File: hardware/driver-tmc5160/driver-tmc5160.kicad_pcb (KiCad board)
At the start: 2 copper layers, 30 x 27 mm, 54 parts, among them M1 Micro-Fit 3.0, T1 GND, T10 STEP, T11 GND, T12 DIR, T13 EN, T16 DIAG0, T17 DIAG1, T18 ENCA, T19 ENCB, T2 CLK, T20 ENCN, T3 12V, T4 SCK, T5 GND, T6 SDI, T7 SDO, T8 VCC, T9 CS0, U1 TMC5160A-TA

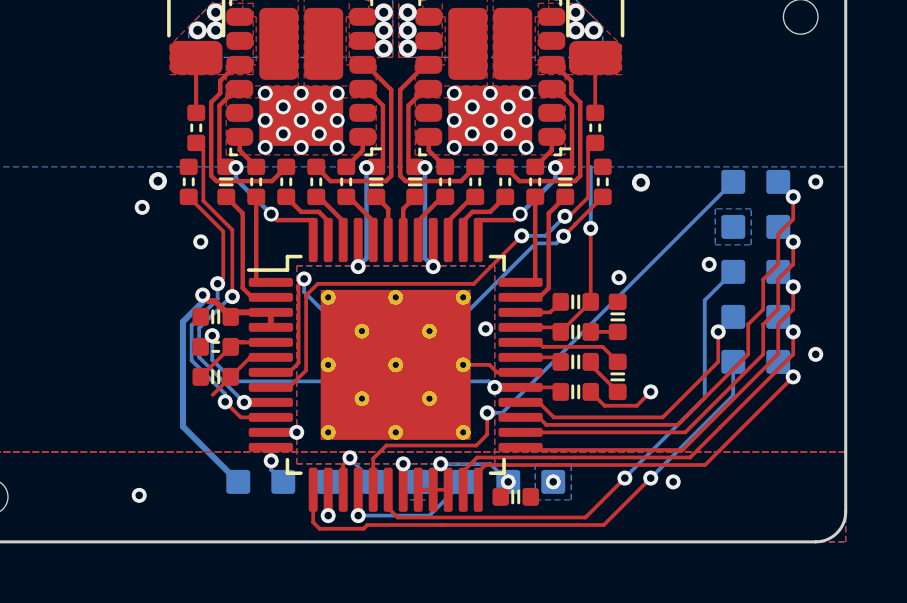
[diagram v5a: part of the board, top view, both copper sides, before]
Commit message: added components and further work on PCB layout design
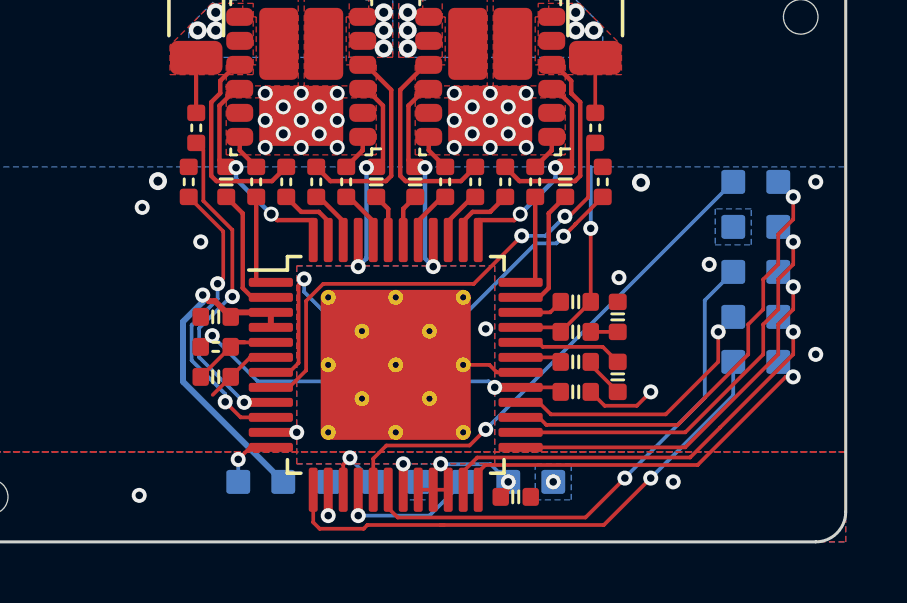
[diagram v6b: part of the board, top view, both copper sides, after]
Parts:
- moved T2 1.50 mm to (129.8, 84.5), turned to 0 degrees
- moved T3 1.50 mm to (131.2, 84.5), turned to 0 degrees
- turned T4 to 0 degrees
- turned T5 to 0 degrees
- turned T6 to 0 degrees
- turned T7 to 0 degrees
- turned T8 to 0 degrees
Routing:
- net +12V: track 10.4 -> 11.0 mm

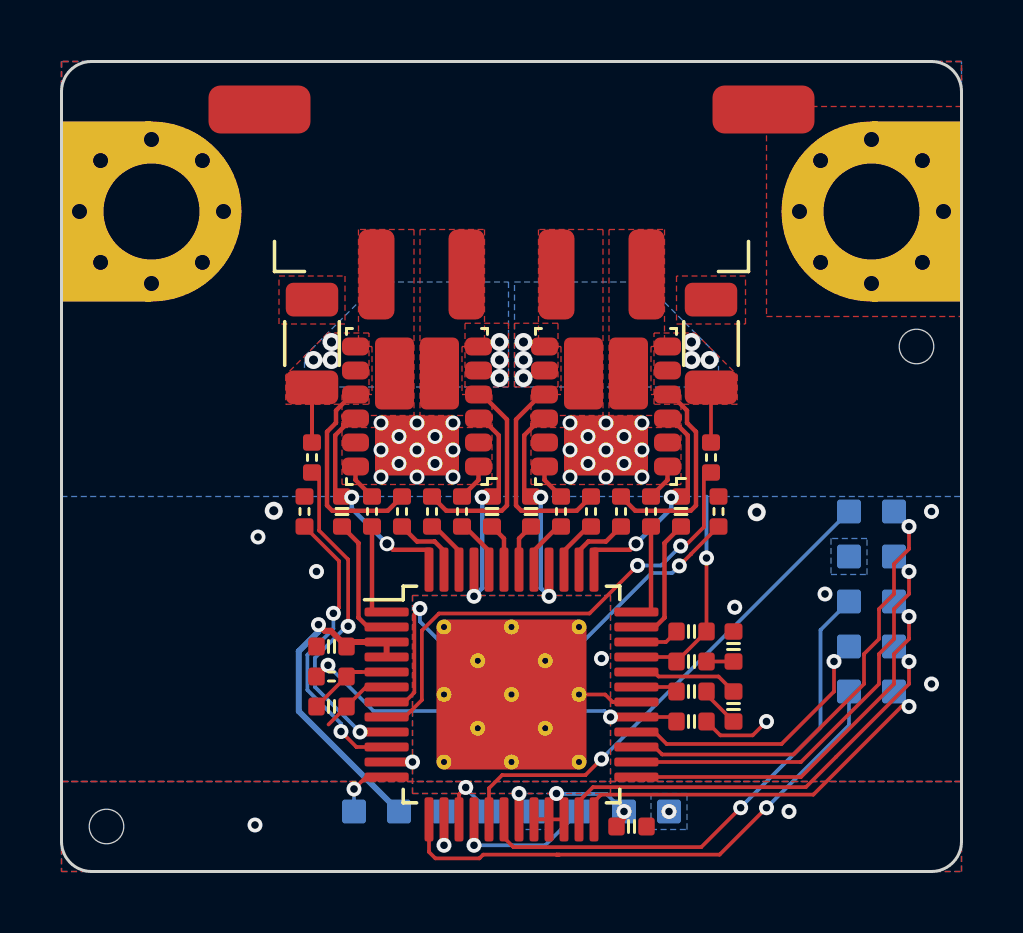
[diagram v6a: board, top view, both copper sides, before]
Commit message: added more 3D models and created first few renders
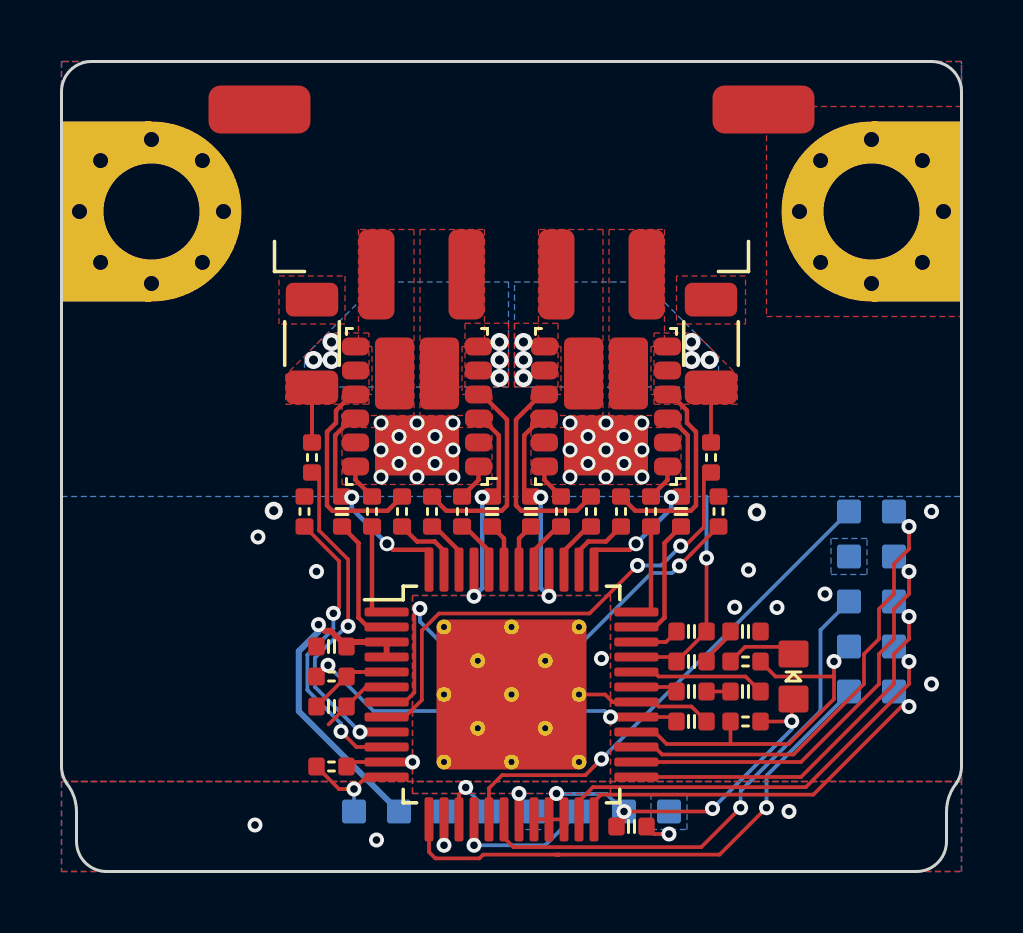
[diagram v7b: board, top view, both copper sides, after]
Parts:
- removed REF** (x2): ToolingHole, corevus:ToolingHole
- added D1: Red, AlphaLib:0603LED, F.Cu at (144.4, 80.0)
- added R16: 10kΩ, AlphaLib:0402R, F.Cu at (129.0, 83.0)
- added R17: 10kΩ, AlphaLib:0402R, F.Cu at (142.8, 81.5)
- added R18: 1kΩ, AlphaLib:0402R, F.Cu at (142.8, 79.5)
- C1, C2: value 2.2μF -> 1μF
- moved C12 0.64 mm to (142.8, 78.5), turned to 0 degrees
- moved C7 0.64 mm to (142.8, 80.5), turned to 180 degrees
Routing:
- net VCC: track 5.16 -> 14.0 mm, vias 2 -> 4
- net /~{En}: track 9.19 -> 12.7 mm
- net GND: track 7.57 -> 10.0 mm, vias 15 -> 17
- net Net-(D1-K): track 0.00 -> 2.45 mm
- net /Clk: track 2.00 -> 3.56 mm
- net Net-(U1-CPI): track 3.51 -> 4.41 mm
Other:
- outline, holes or cut-outs redrawn

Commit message: adopt corevus-g designation for current mainboard, cleanup
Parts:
- added REF**: ToolingHole, corevus:ToolingHole, F.Cu at (122.0, 85.0)
- added REF**: ToolingHole, corevus:ToolingHole, F.Cu at (148.5, 69.0)
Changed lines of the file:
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@@
     (fp_line (start 7.9 5.4) (end 7.9 4.4)
       (stroke (width 0.12) (type solid)) (layer "F.SilkS"))
-    (fp_line (start -10.6 -1.3) (end -10.6 1.3)
-      (stroke (width 0.05) (type solid)) (layer "F.CrtYd"))
-    (fp_line (start -10.6 -1.3) (end -8.3 -1.3)
-      (stroke (width 0.05) (type solid)) (layer "F.CrtYd"))
-    (fp_line (start -10.6 1.3) (end -8.3 1.3)
+    (fp_line (start -9.6 -1.3) (end -9.6 1.3)
+      (stroke (width 0.05) (type solid)) (layer "F.CrtYd"))
+    (fp_line (start -9.6 -1.3) (end -8.3 -1.3)
+      (stroke (width 0.05) (type solid)) (layer "F.CrtYd"))
+    (fp_line (start -9.6 1.3) (end -8.3 1.3)
       (stroke (width 0.05) (type solid)) (layer "F.CrtYd"))
     (fp_line (start -8.3 -1.3) (end -8.3 -5.1)
@@
     (fp_line (start 8.3 5.8) (end 5.6 5.8)
       (stroke (width 0.05) (type solid)) (layer "F.CrtYd"))
-    (fp_line (start 10.6 -1.3) (end 8.3 -1.3)
-      (stroke (width 0.05) (type solid)) (layer "F.CrtYd"))
-    (fp_line (start 10.6 1.3) (end 8.3 1.3)
-      (stroke (width 0.05) (type solid)) (layer "F.CrtYd"))
-    (fp_line (start 10.6 1.3) (end 10.6 -1.3)
+    (fp_line (start 9.6 -1.3) (end 8.3 -1.3)
+      (stroke (width 0.05) (type solid)) (layer "F.CrtYd"))
+    (fp_line (start 9.6 1.3) (end 8.3 1.3)
+      (stroke (width 0.05) (type solid)) (layer "F.CrtYd"))
+    (fp_line (start 9.6 1.3) (end 9.6 -1.3)
       (stroke (width 0.05) (type solid)) (layer "F.CrtYd"))
     (fp_line (start -7.8 -3.2) (end -7.8 5.3)
@@
     (pad "4" smd roundrect (at 4.5 5.5) (size 1.2 3) (layers "F.Cu" "F.Paste" "F.Mask") (roundrect_rratio 0.25)
       (net 22 "/Motor_A2") (pintype "passive"))
-    (pad "MP" smd roundrect (at -8.4 0) (size 3.4 1.6) (layers "F.Cu" "F.Paste" "F.Mask") (roundrect_rratio 0.25))
-    (pad "MP" smd roundrect (at 8.4 0) (size 3.4 1.6) (layers "F.Cu" "F.Paste" "F.Mask") (roundrect_rratio 0.25))
-    (model "${KICAD6_3DMODEL_DIR}/Connector_Molex.3dshapes/Molex_Micro-Fit_3.0_43650-0424_1x04-1MP_P3.00mm_Vertical.wrl"
-      (offset (xyz 0 0 0))
-      (scale (xyz 1 1 1))
-      (rotate (xyz 0 0 0))
+    (pad "MP" smd roundrect (at -7.75 0) (size 3 1.8) (layers "F.Cu" "F.Paste" "F.Mask") (roundrect_rratio 0.25))
+    (pad "MP" smd roundrect (at 7.75 0) (size 3 1.8) (layers "F.Cu" "F.Paste" "F.Mask") (roundrect_rratio 0.25))
+    (model "${COREVUS}/lib/corevus.3dshapes/CONN-SMD_1x4P-L15.7-W9.9-H3.9-P3.0.wrl"
+      (offset (xyz 4.5 -4.25 0.5))
+      (scale (xyz 1 1 1))
+      (rotate (xyz 0 0 180))
     )
   )
@@
       (rotate (xyz 0 0 0))
     )
+  )
+  (footprint "corevus:ToolingHole" (layer "F.Cu")
+    (at 122 85)
+    (attr through_hole)
+    (fp_text reference "REF**" (at 0 -1.25 unlocked) (layer "F.SilkS") hide
+        (effects (font (size 1 1) (thickness 0.15)))
+    )
+    (fp_text value "ToolingHole" (at 0 1 unlocked) (layer "F.Fab")
+        (effects (font (size 1 1) (thickness 0.15)))
+    )
+    (fp_text user "${REFERENCE}" (at 0 2.5 unlocked) (layer "F.Fab")
+        (effects (font (size 1 1) (thickness 0.15)))
+    )
+    (pad "" np_thru_hole circle (at 0 0) (size 1.3 1.3) (drill 1.152) (layers "*.Mask"))
   )
   (footprint "AlphaLib:0402R" (layer "F.Cu")
@@
     )
   )
+  (footprint "corevus:ToolingHole" (layer "F.Cu")
+    (at 148.5 69)
+    (attr through_hole)
+    (fp_text reference "REF**" (at 0 -1.25 unlocked) (layer "F.SilkS") hide
+        (effects (font (size 1 1) (thickness 0.15)))
+    )
+    (fp_text value "ToolingHole" (at 0 1 unlocked) (layer "F.Fab")
+        (effects (font (size 1 1) (thickness 0.15)))
+    )
+    (fp_text user "${REFERENCE}" (at 0 2.5 unlocked) (layer "F.Fab")
+        (effects (font (size 1 1) (thickness 0.15)))
+    )
+    (pad "" np_thru_hole circle (at 0 0) (size 1.3 1.3) (drill 1.152) (layers "*.Mask"))
+  )
   (footprint "AlphaLib:0402C" (layer "F.Cu")
